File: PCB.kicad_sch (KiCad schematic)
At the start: 17 parts, among them J1 Conector IR, J10 Conector ultrassonico esquerdo, J11 Conector ultrassonico central, J12 Conector ultrassonico direito, J13 Conector LED Extra, J14 Conector LORA, J15 ENCO_SW_Esq, J16 ENCO_SW_Dir, J18 LEDs, J2 Conector bluetooth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

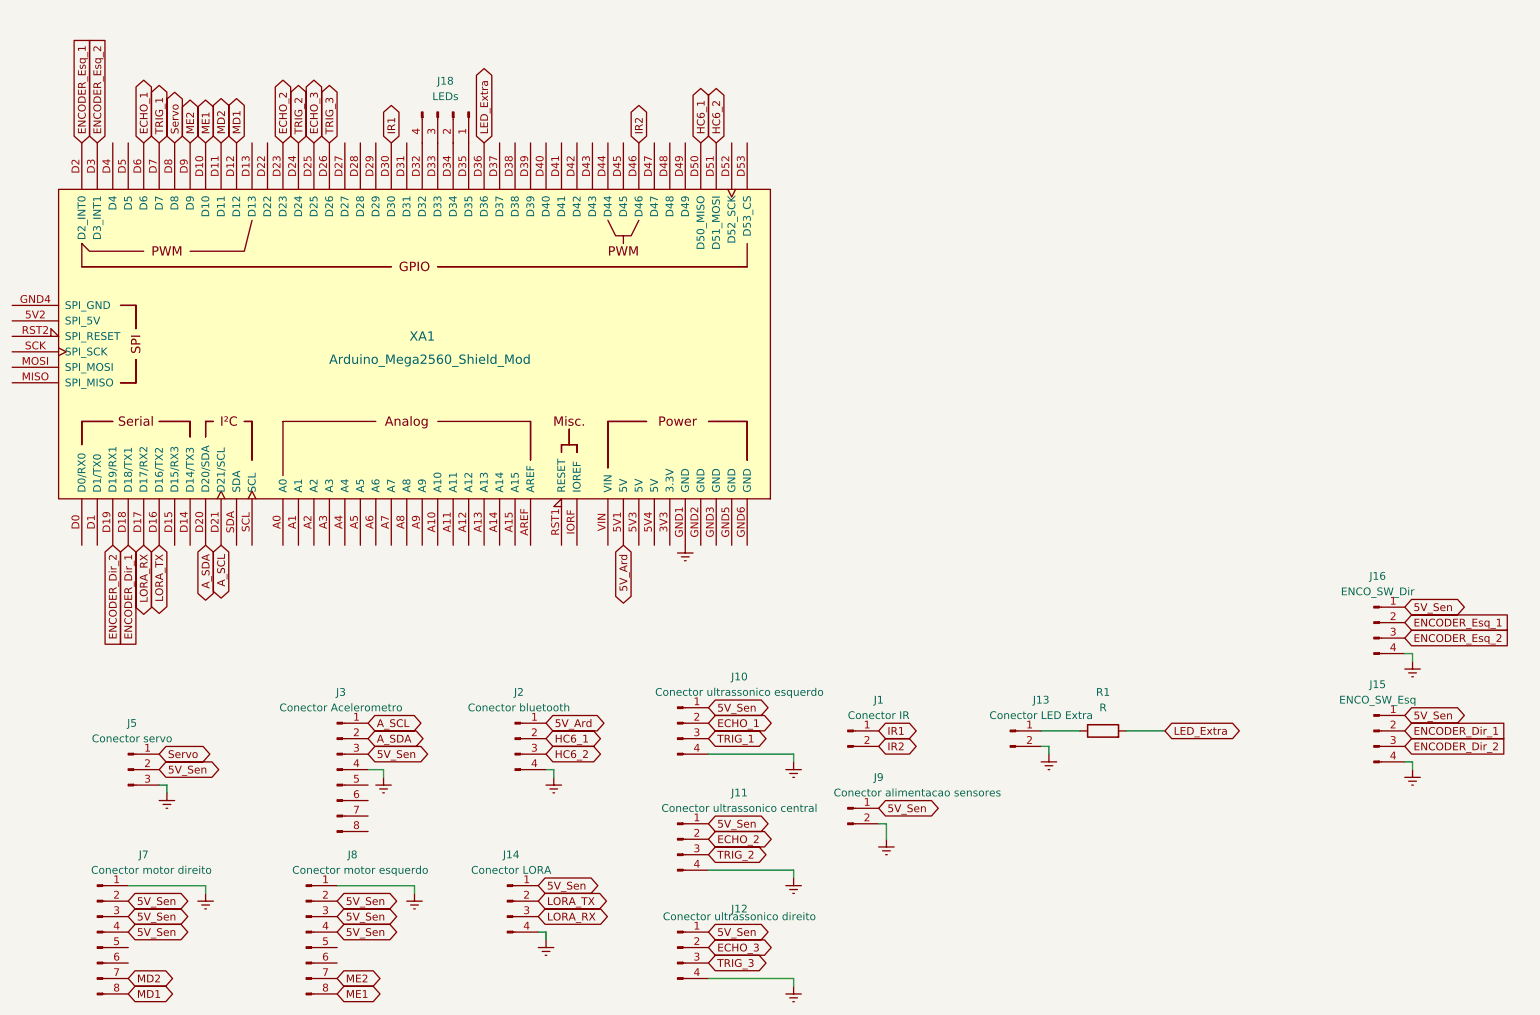
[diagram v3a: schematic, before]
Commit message: fix: mudanca esquematico leds farois
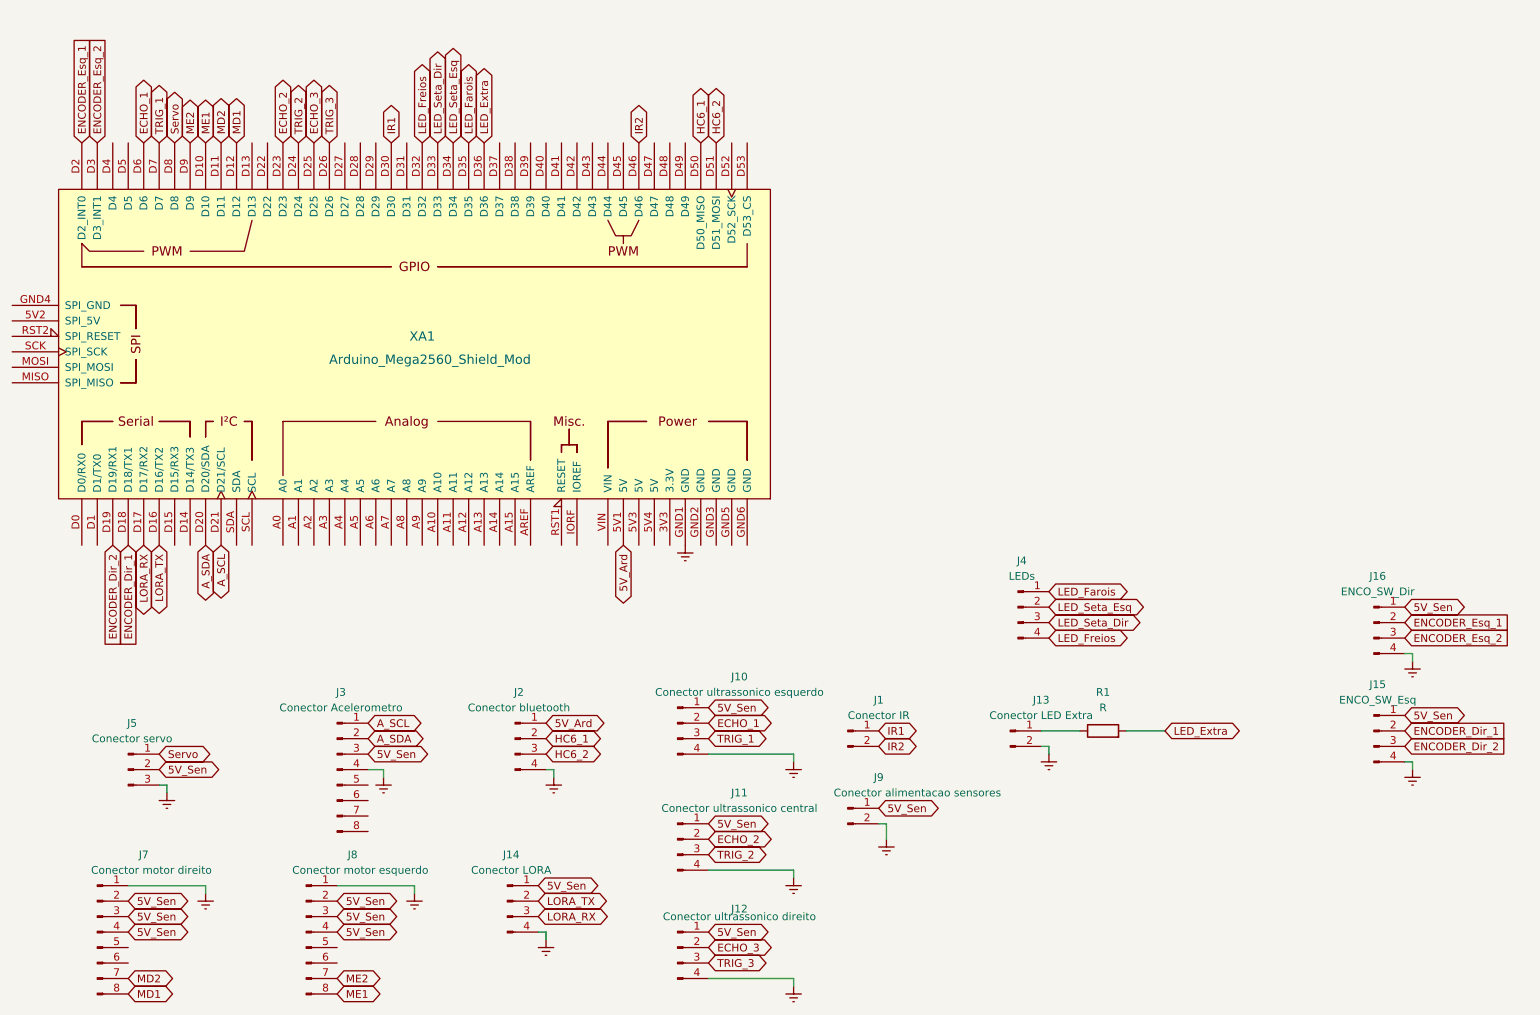
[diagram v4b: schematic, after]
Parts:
- removed J18: LEDs, TerminalBlock_Phoenix:TerminalBlock_Phoenix_MKDS-1,5-4_1x04_P5.00mm_Horizontal, symbol Connector:Conn_01x04_Pin
- added J4: LEDs, TerminalBlock_Phoenix:TerminalBlock_Phoenix_MKDS-1,5-4_1x04_P5.00mm_Horizontal, symbol Connector:Conn_01x04_Pin
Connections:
- net LED_Freios: now reaches XA1.D32
- net LED_Freios: now also J4.4 (Pin_4)
- net LED_Seta_Dir: now reaches XA1.D33
- net LED_Seta_Dir: now also J4.3 (Pin_3)
- net LED_Seta_Esq: now reaches XA1.D34
- net LED_Seta_Esq: now also J4.2 (Pin_2)
- net LED_Farois: now reaches XA1.D35
- net LED_Farois: now also J4.1 (Pin_1)
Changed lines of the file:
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@@
+    )
+  )
+  (global_label "LED_Freios" (shape bidirectional) (at 194.31 128.27 0) (fields_autoplaced)
+    (effects (font (size 1.27 1.27)) (justify left))
+    (property "Intersheetrefs" "${INTERSHEET_REFS}" (at 208.5665 128.27 0)
+      (effects (font (size 1.27 1.27)) (justify left) hide)
     )
   )
@@
     )
   )
+  (global_label "LED_Farois" (shape bidirectional) (at 194.31 120.65 0) (fields_autoplaced)
+    (effects (font (size 1.27 1.27)) (justify left))
+    (property "Intersheetrefs" "${INTERSHEET_REFS}" (at 208.6269 120.65 0)
+      (effects (font (size 1.27 1.27)) (justify left) hide)
+    )
+  )
   (global_label "LED_Extra" (shape bidirectional) (at 101.6 46.99 90) (fields_autoplaced)
     (effects (font (size 1.27 1.27)) (justify left))
@@
     )
   )
+  (global_label "LED_Seta_Dir" (shape bidirectional) (at 93.98 46.99 90) (fields_autoplaced)
+    (effects (font (size 1.27 1.27)) (justify left))
+    (property "Intersheetrefs" "${INTERSHEET_REFS}" (at 93.98 30.6774 90)
+      (effects (font (size 1.27 1.27)) (justify left) hide)
+    )
+  )
   (global_label "5V_Sen" (shape bidirectional) (at 48.26 149.86 0) (fields_autoplaced)
     (effects (font (size 1.27 1.27)) (justify left))
@@
     (effects (font (size 1.27 1.27)) (justify left))
     (property "Intersheetrefs" "${INTERSHEET_REFS}" (at 93.3593 147.32 0)
+      (effects (font (size 1.27 1.27)) (justify left) hide)
+    )
+  )
+  (global_label "LED_Seta_Esq" (shape bidirectional) (at 194.31 123.19 0) (fields_autoplaced)
+    (effects (font (size 1.27 1.27)) (justify left))
+    (property "Intersheetrefs" "${INTERSHEET_REFS}" (at 211.2877 123.19 0)
       (effects (font (size 1.27 1.27)) (justify left) hide)
     )
@@
     )
   )
+  (global_label "LED_Freios" (shape bidirectional) (at 91.44 46.99 90) (fields_autoplaced)
+    (effects (font (size 1.27 1.27)) (justify left))
+    (property "Intersheetrefs" "${INTERSHEET_REFS}" (at 91.44 32.7335 90)
+      (effects (font (size 1.27 1.27)) (justify left) hide)
+    )
+  )
   (global_label "LORA_RX" (shape bidirectional) (at 45.72 113.03 270) (fields_autoplaced)
     (effects (font (size 1.27 1.27)) (justify right))
@@
     )
   )
+  (global_label "LED_Seta_Esq" (shape bidirectional) (at 96.52 46.99 90) (fields_autoplaced)
+    (effects (font (size 1.27 1.27)) (justify left))
+    (property "Intersheetrefs" "${INTERSHEET_REFS}" (at 96.52 30.0123 90)
+      (effects (font (size 1.27 1.27)) (justify left) hide)
+    )
+  )
   (global_label "ECHO_3" (shape bidirectional) (at 73.66 46.99 90) (fields_autoplaced)
     (effects (font (size 1.27 1.27)) (justify left))
@@
     (effects (font (size 1.27 1.27)) (justify left))
     (property "Intersheetrefs" "${INTERSHEET_REFS}" (at 92.2103 142.24 0)
+      (effects (font (size 1.27 1.27)) (justify left) hide)
+    )
+  )
+  (global_label "LED_Seta_Dir" (shape bidirectional) (at 194.31 125.73 0) (fields_autoplaced)
+    (effects (font (size 1.27 1.27)) (justify left))
+    (property "Intersheetrefs" "${INTERSHEET_REFS}" (at 210.6226 125.73 0)
       (effects (font (size 1.27 1.27)) (justify left) hide)
     )
@@
     (effects (font (size 1.27 1.27)) (justify left))
     (property "Intersheetrefs" "${INTERSHEET_REFS}" (at 51.2074 184.15 0)
+      (effects (font (size 1.27 1.27)) (justify left) hide)
+    )
+  )
+  (global_label "LED_Farois" (shape bidirectional) (at 99.06 46.99 90) (fields_autoplaced)
+    (effects (font (size 1.27 1.27)) (justify left))
+    (property "Intersheetrefs" "${INTERSHEET_REFS}" (at 99.06 32.6731 90)
       (effects (font (size 1.27 1.27)) (justify left) hide)
     )
@@
     )
   )
-  (symbol (lib_id "Connector:Conn_01x04_Pin") (at 96.52 41.91 270) (unit 1)
+  (symbol (lib_id "power:Earth") (at 254 149.86 0) (unit 1)
     (in_bom yes) (on_board yes) (dnp no) (fields_autoplaced)
-    (property "Reference" "J18" (at 95.25 36.83 90)
-      (effects (font (size 1.27 1.27)))
-    )
-    (property "Value" "LEDs" (at 95.25 39.37 90)
-      (effects (font (size 1.27 1.27)))
-    )
-    (property "Footprint" "TerminalBlock_Phoenix:TerminalBlock_Phoenix_MKDS-1,5-4_1x04_P5.00mm_Horizontal" (at 96.52 41.91 0)
-      (effects (font (size 1.27 1.27)) hide)
-    )
-    (property "Datasheet" "~" (at 96.52 41.91 0)
+    (property "Reference" "#PWR014" (at 254 156.21 0)
+      (effects (font (size 1.27 1.27)) hide)
+    )
+    (property "Value" "Earth" (at 254 153.67 0)
+      (effects (font (size 1.27 1.27)) hide)
+    )
+    (property "Footprint" "" (at 254 149.86 0)
+      (effects (font (size 1.27 1.27)) hide)
+    )
+    (property "Datasheet" "~" (at 254 149.86 0)
+      (effects (font (size 1.27 1.27)) hide)
+    )
+    (pin "1")
+    (instances
+      (project "PCB"
+        (path "/b344186f-9059-49c5-a6f7-f90c862ad97f"
+          (reference "#PWR014") (unit 1)
+        )
+      )
+      (project "esquemaEletricoCarro"
+        (path "/e63e39d7-6ac0-4ffd-8aa3-1841a4541b55/ef1da815-5ae9-4f7a-859c-d7960e6acc1e"
+          (reference "#PWR021") (unit 1)
+        )
+      )
+    )
+  )
+  (symbol (lib_id "Connector:Conn_01x04_Pin") (at 133.35 179.07 0) (unit 1)
+    (in_bom yes) (on_board yes) (dnp no)
+    (property "Reference" "J12" (at 143.51 172.72 0)
+      (effects (font (size 1.27 1.27)))
+    )
+    (property "Value" "Conector ultrassonico direito" (at 143.51 173.99 0)
+      (effects (font (size 1.27 1.27)))
+    )
+    (property "Footprint" "Connector_JST:JST_XH_B4B-XH-A_1x04_P2.50mm_Vertical" (at 133.35 179.07 0)
+      (effects (font (size 1.27 1.27)) hide)
+    )
+    (property "Datasheet" "~" (at 133.35 179.07 0)
       (effects (font (size 1.27 1.27)) hide)
     )
@@
       (project "PCB"
         (path "/b344186f-9059-49c5-a6f7-f90c862ad97f"
-          (reference "J18") (unit 1)
-        )
-      )
-    )
-  )
-  (symbol (lib_id "power:Earth") (at 254 149.86 0) (unit 1)
+          (reference "J12") (unit 1)
+        )
+      )
+    )
+  )
+  (symbol (lib_id "Connector:Conn_01x04_Pin") (at 189.23 123.19 0) (unit 1)
     (in_bom yes) (on_board yes) (dnp no) (fields_autoplaced)
-    (property "Reference" "#PWR014" (at 254 156.21 0)
-      (effects (font (size 1.27 1.27)) hide)
-    )
-    (property "Value" "Earth" (at 254 153.67 0)
-      (effects (font (size 1.27 1.27)) hide)
-    )
-    (property "Footprint" "" (at 254 149.86 0)
-      (effects (font (size 1.27 1.27)) hide)
-    )
-    (property "Datasheet" "~" (at 254 149.86 0)
-      (effects (font (size 1.27 1.27)) hide)
-    )
-    (pin "1")
-    (instances
-      (project "PCB"
-        (path "/b344186f-9059-49c5-a6f7-f90c862ad97f"
-          (reference "#PWR014") (unit 1)
-        )
-      )
-      (project "esquemaEletricoCarro"
-        (path "/e63e39d7-6ac0-4ffd-8aa3-1841a4541b55/ef1da815-5ae9-4f7a-859c-d7960e6acc1e"
-          (reference "#PWR021") (unit 1)
-        )
-      )
-    )
-  )
-  (symbol (lib_id "Connector:Conn_01x04_Pin") (at 133.35 179.07 0) (unit 1)
-    (in_bom yes) (on_board yes) (dnp no)
-    (property "Reference" "J12" (at 143.51 172.72 0)
-      (effects (font (size 1.27 1.27)))
-    )
-    (property "Value" "Conector ultrassonico direito" (at 143.51 173.99 0)
-      (effects (font (size 1.27 1.27)))
-    )
-    (property "Footprint" "Connector_JST:JST_XH_B4B-XH-A_1x04_P2.50mm_Vertical" (at 133.35 179.07 0)
-      (effects (font (size 1.27 1.27)) hide)
-    )
-    (property "Datasheet" "~" (at 133.35 179.07 0)
+    (property "Reference" "J4" (at 189.865 115.57 0)
+      (effects (font (size 1.27 1.27)))
+    )
+    (property "Value" "LEDs" (at 189.865 118.11 0)
+      (effects (font (size 1.27 1.27)))
+    )
+    (property "Footprint" "TerminalBlock_Phoenix:TerminalBlock_Phoenix_MKDS-1,5-4_1x04_P5.00mm_Horizontal" (at 189.23 123.19 0)
+      (effects (font (size 1.27 1.27)) hide)
+    )
+    (property "Datasheet" "~" (at 189.23 123.19 0)
       (effects (font (size 1.27 1.27)) hide)
     )
@@
       (project "PCB"
         (path "/b344186f-9059-49c5-a6f7-f90c862ad97f"
-          (reference "J12") (unit 1)
-        )
-      )
+          (reference "J4") (unit 1)
+        )
+      )
